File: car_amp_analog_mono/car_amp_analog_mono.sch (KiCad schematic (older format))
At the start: 15 parts, among them U1 L7805, U2 NE5532

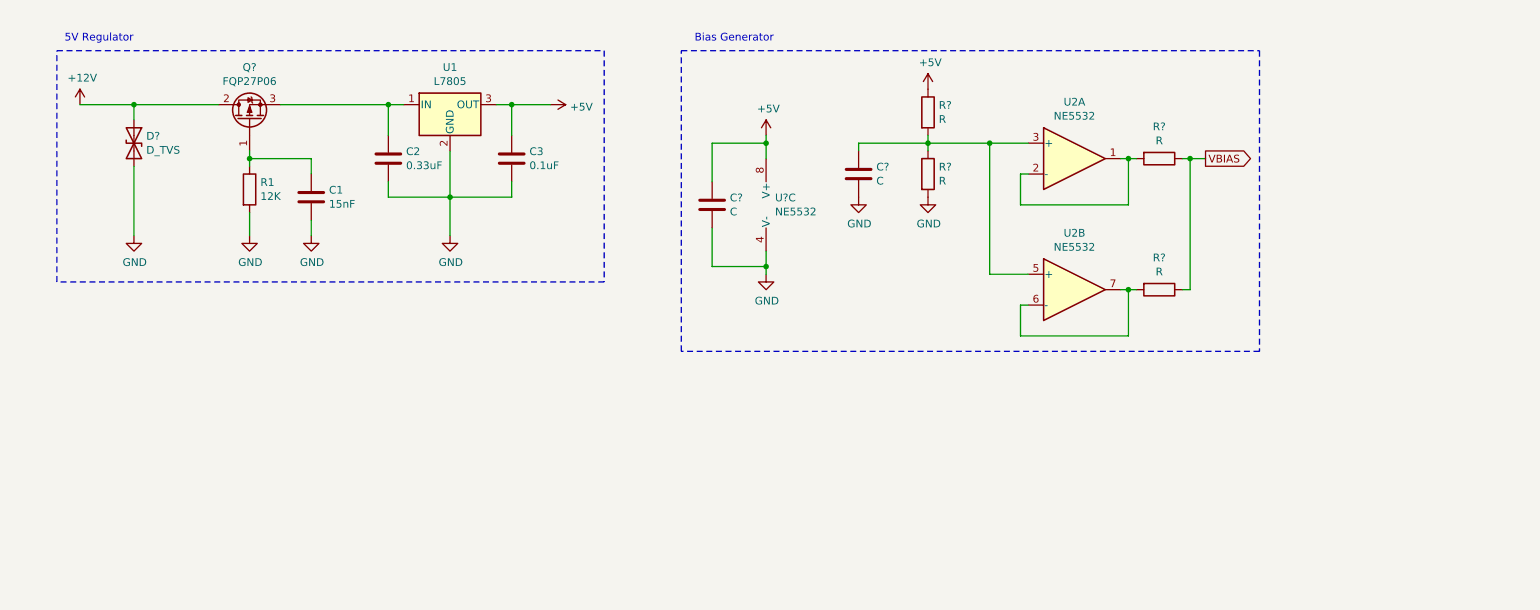
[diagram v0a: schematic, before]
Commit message: Add values to components and minor changes
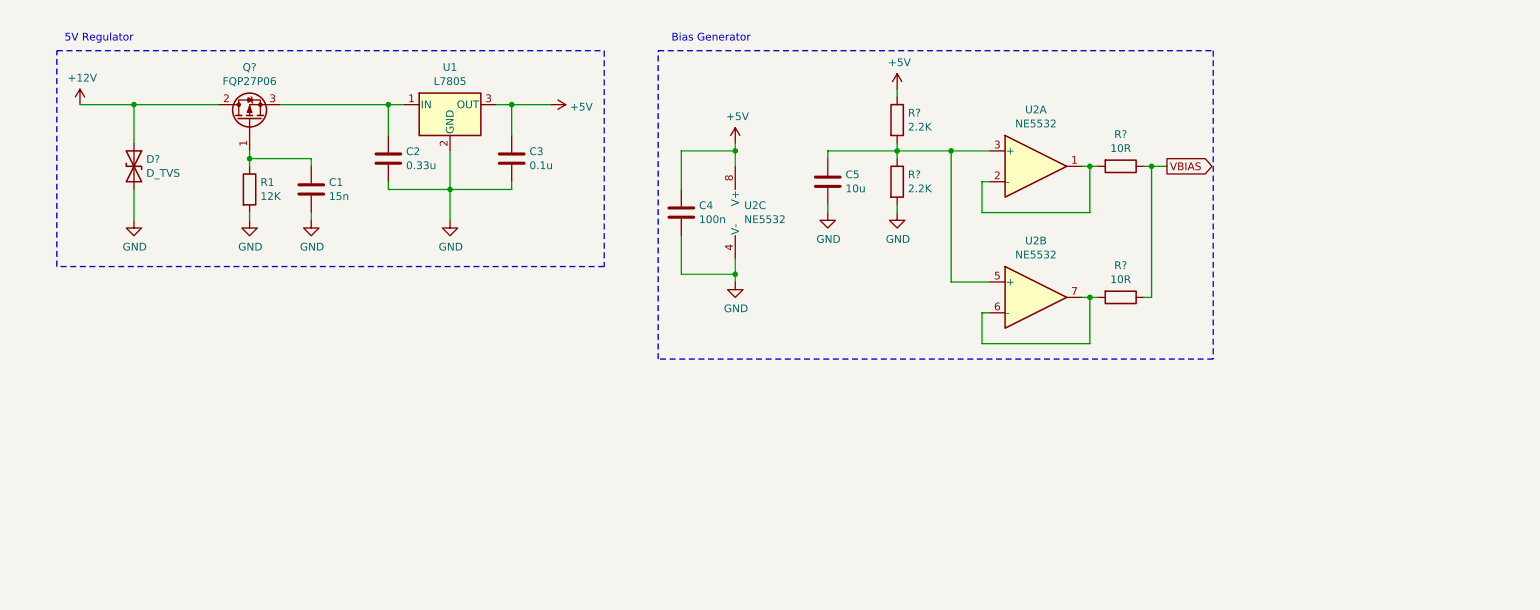
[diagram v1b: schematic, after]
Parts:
- C1: value 15nF -> 15n
- C2: value 0.33uF -> 0.33u
- C3: value 0.1uF -> 0.1u
- C4: renamed from C?; value C -> 100n
- C5: renamed from C?; value C -> 10u
- R? (x2): value R -> 10R
- R? (x2): value R -> 2.2K
- gave numbers to parts that had none: 1
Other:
- moved on the sheet: C1, C4, C5, D?, R?, U2A, U2B, U2C

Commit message: Add ignition logic
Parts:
- added C?: C, symbol Device:C
- added D?: D_Zener, symbol Device:D_Zener
- added R?: 3.3K, symbol Device:R
- added R?: 1.1K, symbol Device:R
- added U?: ATmega328P-PU, Package_DIP:DIP-28_W7.62mm, symbol MCU_Microchip_ATmega:ATmega328P-PU
- added U?: LM321, Package_TO_SOT_SMD:SOT-23-5, symbol Amplifier_Operational:LM321
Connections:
- net labels added: IGNITION, IGNITION_LOGIC
- wire segments 57 -> 74
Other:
- note added: "Ignition"
- moved on the sheet: C1, C2, C3, C4, C5, D?, Q?, R1, R?, U1, U2A, U2B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
